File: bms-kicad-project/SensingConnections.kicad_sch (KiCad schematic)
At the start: 33 parts, among them J10 XT60PW-F, J11 XT60PW-F, J12 1053131303, J13 SM06B-GHS-TB, J14 XT60PW-F, J15 1053131302, J16 1053131302, J17 1053131302, J18 1053131302, J6 XT60PW-F, J7 XT60PW-M, J8 XT60PW-F, J9 5024940670, U7 ACS72981KLRATR-150B5

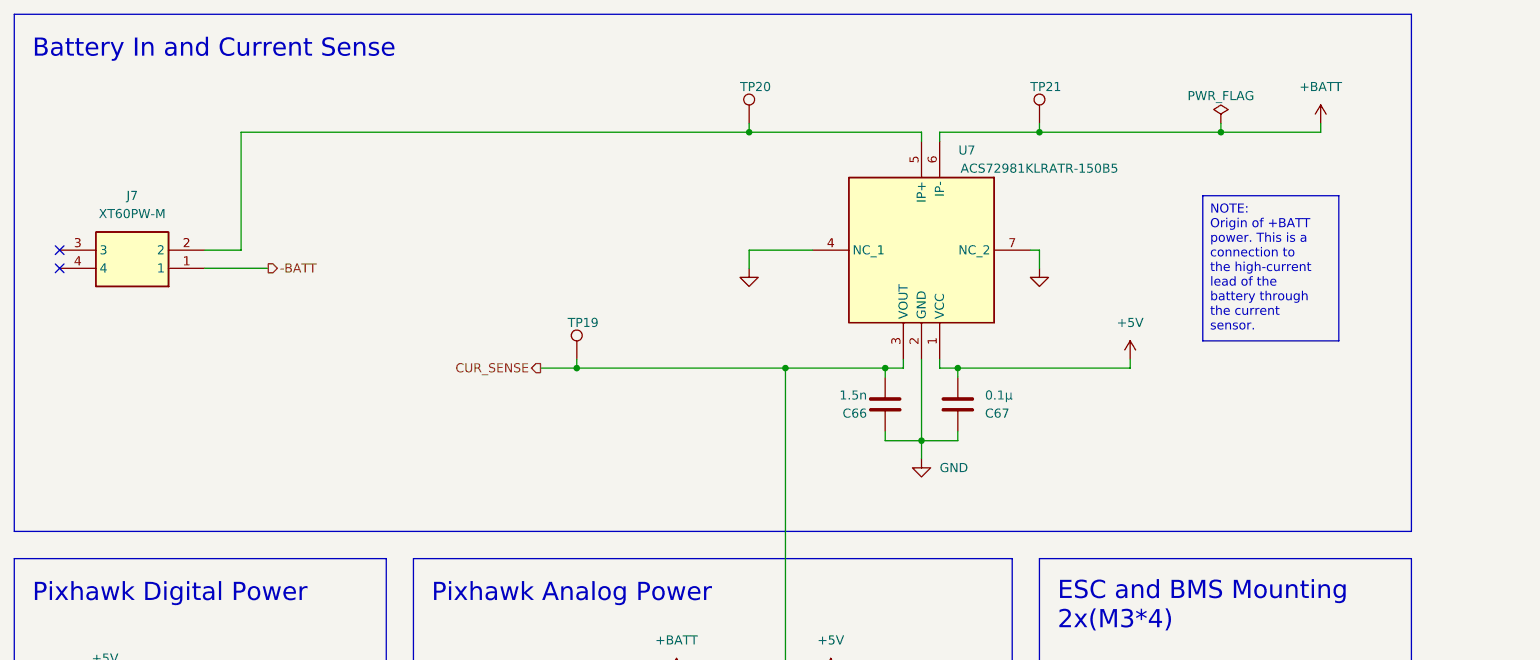
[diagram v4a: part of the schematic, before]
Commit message: feat: added current sense DAC
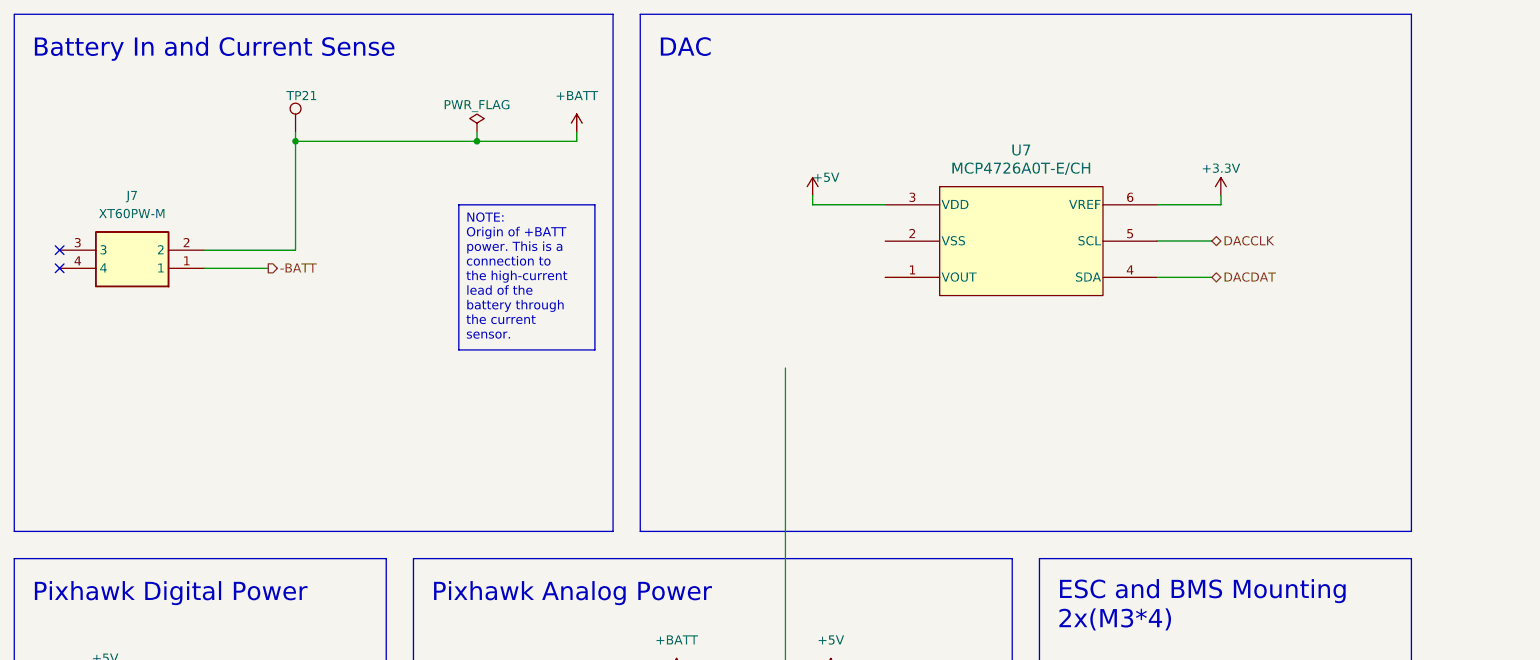
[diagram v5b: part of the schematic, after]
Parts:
- removed C66: 1.5n, FixedWing:G-21_MUR, symbol FixedWing:GRM2165C1H152JA01D
- removed C67: 0.1µ, FixedWing:CAP_GCJ-18_MUR, symbol FixedWing:GCJ188R72A104KA01D
- removed TP19, TP20: TestPoint, TestPoint:TestPoint_Pad_D1.5mm, symbol Connector:TestPoint
- removed U7: ACS72981KLRATR-150B5, FixedWing:ACS780LLRTR050BT, symbol FixedWing:ACS72981KLRATR-150B5
- added U7: MCP4726A0T-E/CH, FixedWing:SOT-23-6_MC_MCH, symbol FixedWing:MCP4726A0T-E_CH
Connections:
- net +5V: now also U7.3 (VDD)
- net +BATT: now also J7.2
- net CUR_SENSE: no longer names the net of J13.3
- new net +3.3V: U7.6 (VREF)
- new net DACCLK: U7.5 (SCL)
- new net DACDAT: U7.4 (SDA)
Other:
- note added: "DAC"
- moved on the sheet: TP21

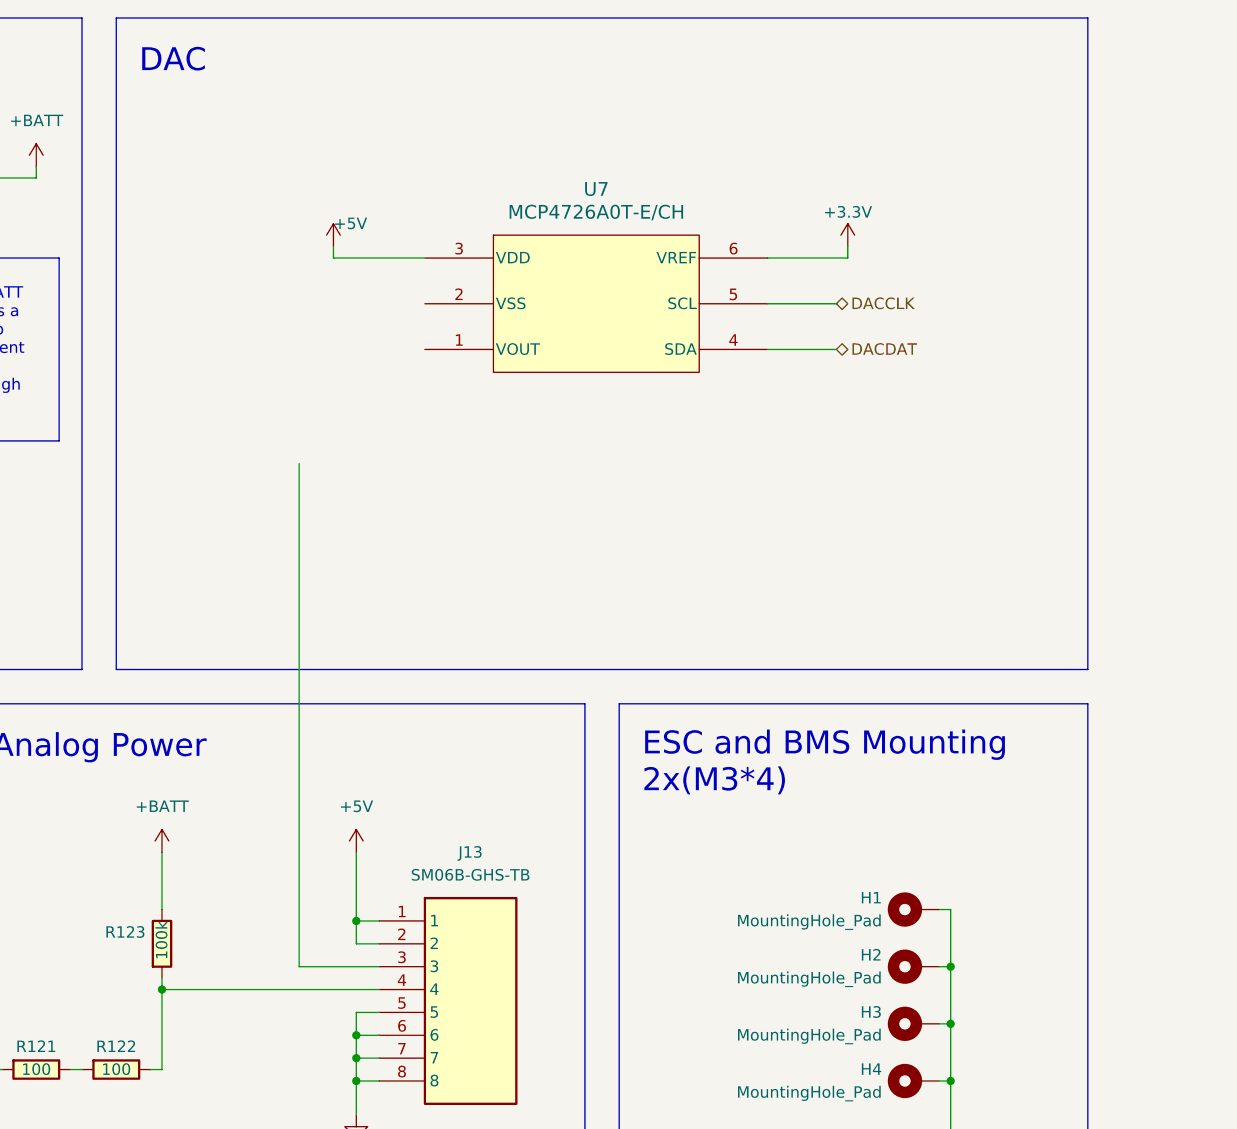
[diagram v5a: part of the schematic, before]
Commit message: feat: added capacitors to DAC
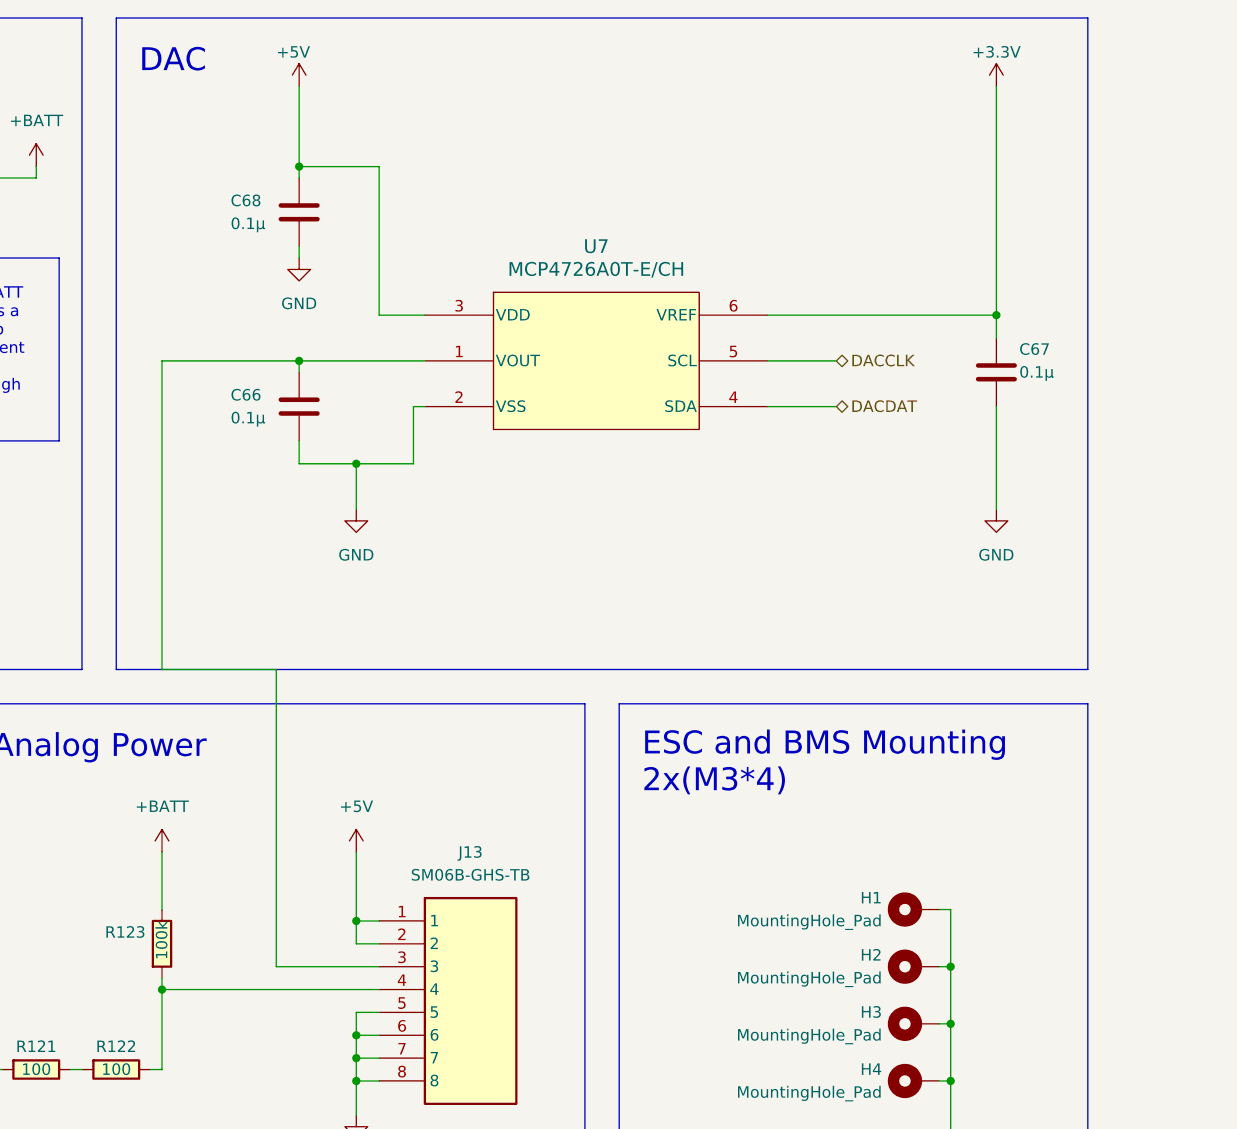
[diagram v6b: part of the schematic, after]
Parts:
- added C66, C67, C68: 0.1µ, FixedWing:CAP_GCJ-18_MUR, symbol FixedWing:GCJ188R72A104KA01D
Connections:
- net +3.3V: now also C67.2
- net +5V: now also C68.2
- net GND: now also U7.2 (VSS), C66.1, C67.1, C68.1
- net at J13.3: now also U7.1 (VOUT), C66.2
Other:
- moved on the sheet: U7

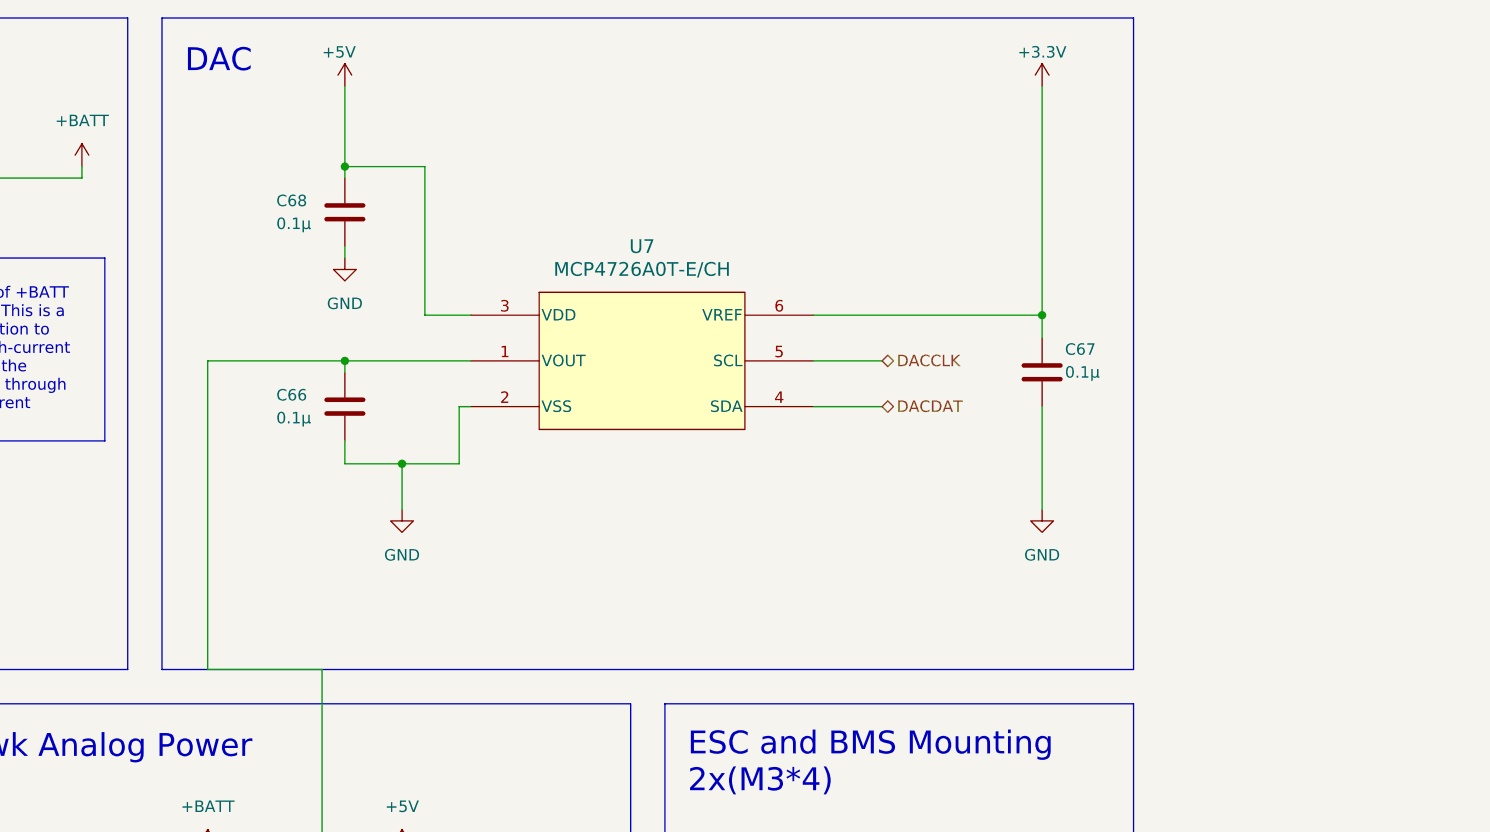
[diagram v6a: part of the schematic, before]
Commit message: feat: more DAC capacitors
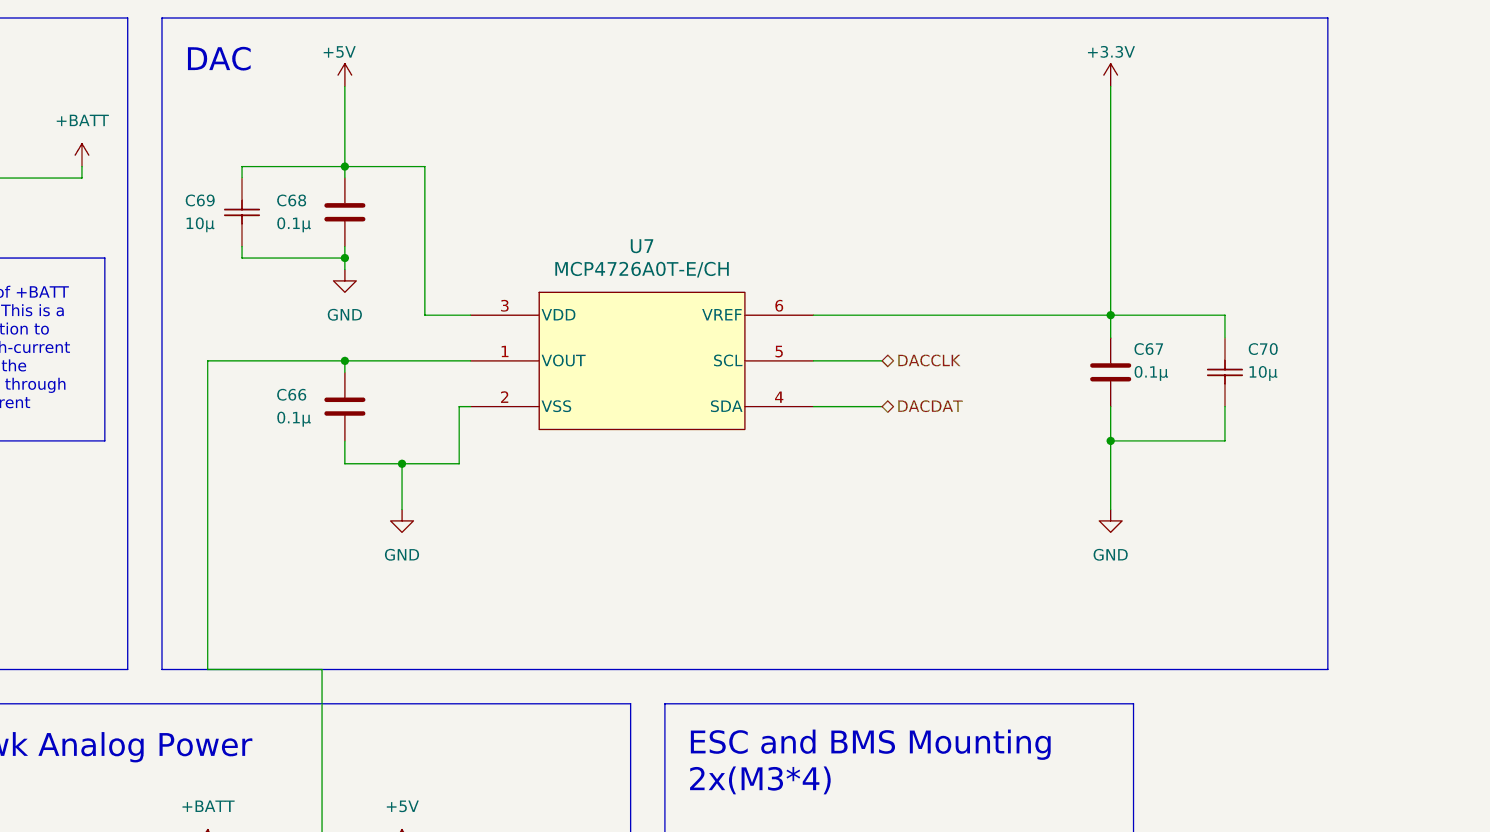
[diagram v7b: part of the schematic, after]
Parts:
- added C69, C70: 10µ, FixedWing:CAP_CL21B106KOQNNNE_SAM, symbol FixedWing:CL21B106KOQNNNE
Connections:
- net +3.3V: now also C70.2
- net +5V: now also C69.2
- net GND: now also C69.1, C70.1
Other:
- moved on the sheet: C67

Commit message: feat: Added temp sensors
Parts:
- added C71, C72: 1µ, FixedWing:CAPC1608X90N, symbol FixedWing:GCM188R71C105KA64D
- added R124, R125, R126, R127: 100, RESC2012X50N, symbol FixedWing:CRCW0805100RFKEA
- added U8, U9: MCP9700AT-E/TT, FixedWing:SOT-23_MC_MCH, symbol FixedWing:MCP9700AT-E_TT
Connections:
- net +5V: now also R124.1, R126.1
- net GND: now also C71.1, C72.1, U8.3 (GND), U9.3 (GND)
- new net: R124.2, R125.1
- new net: C72.2, R127.2, U8.1 (VDD)
- new net: C71.2, R125.2, U9.1 (VDD)
- new net: R126.2, R127.1
- new net TEMP_BAL: U9.2 (VOUT)
- new net TEMP_CORE: U8.2 (VOUT)
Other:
- note added: "Temperature Sensors"
- moved on the sheet: C66, C67, C68, C69, C70, H1, H2, H3, H4, H5, H6, H7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
